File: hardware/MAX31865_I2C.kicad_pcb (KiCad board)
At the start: 2 copper layers, 25.4 x 27.9 mm, 3 parts

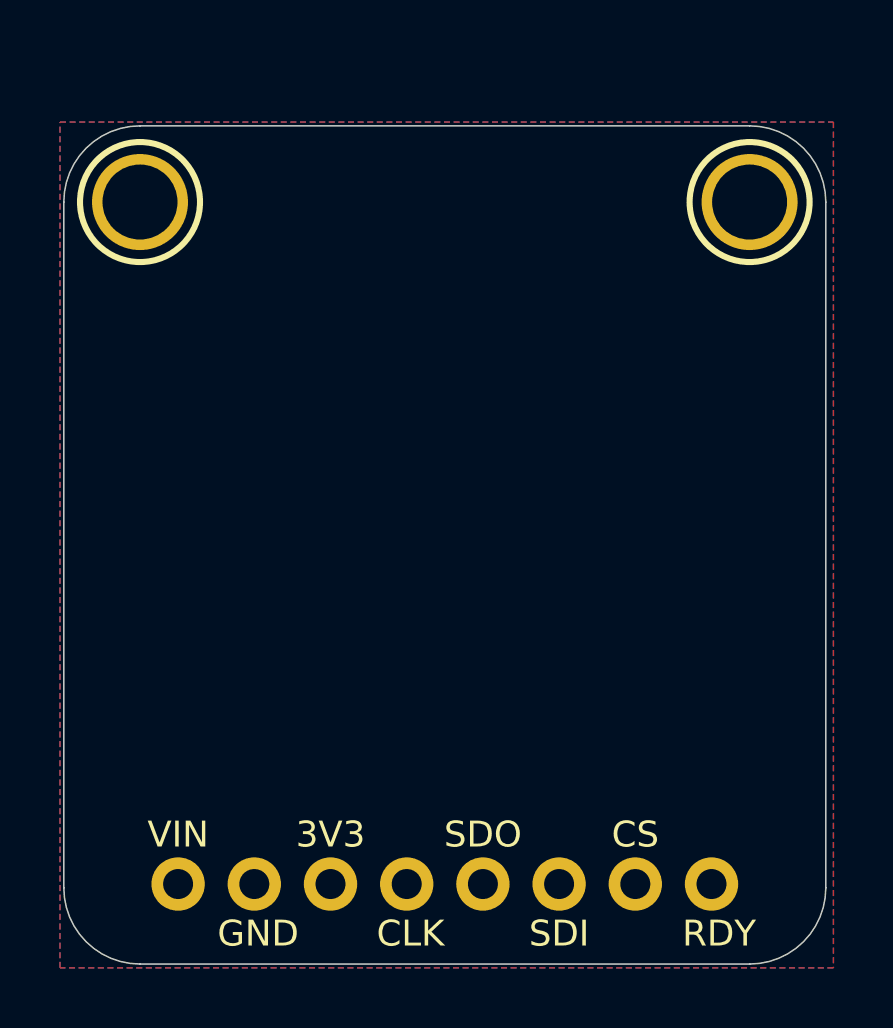
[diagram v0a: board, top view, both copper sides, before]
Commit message: added rough sketch of the adapter PCB
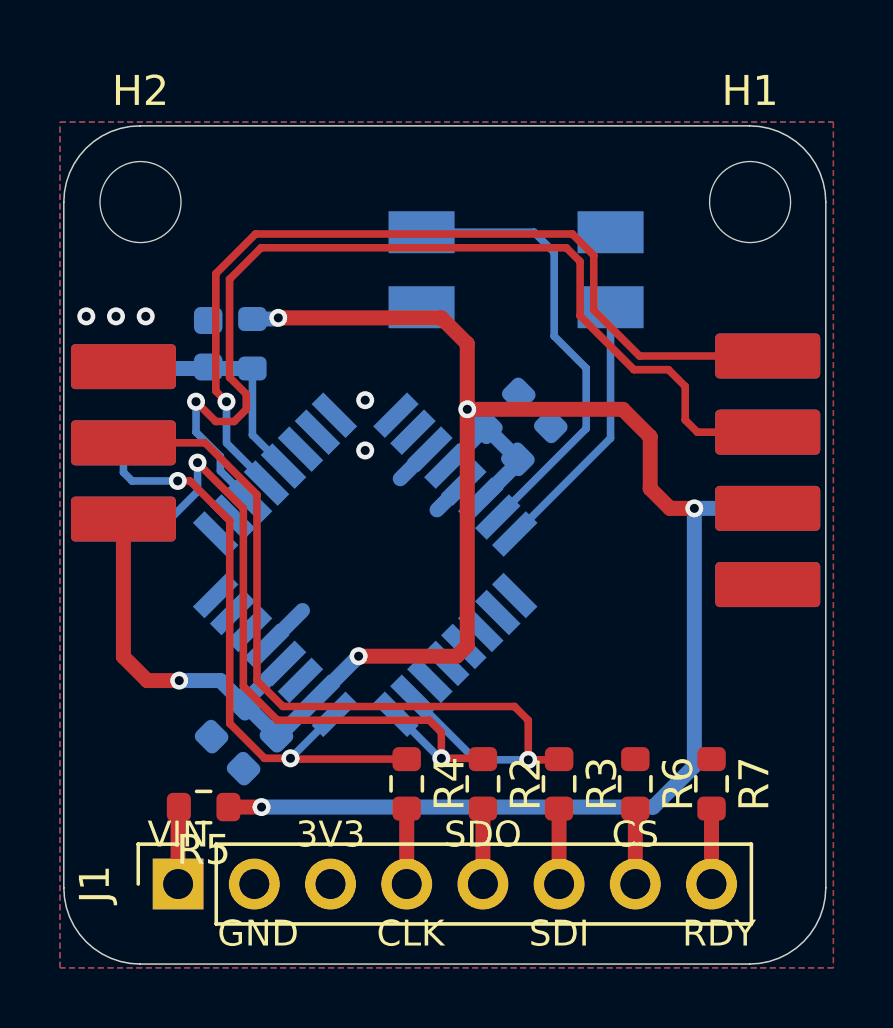
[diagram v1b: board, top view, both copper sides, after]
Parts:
- removed JP1: , 1X08_ROUND_70
- removed U$18, U$19: MOUNTINGHOLE2.5, MOUNTINGHOLE_2.5_PLATED
- added C1: 100n, Capacitor_SMD:C_0603_1608Metric, B.Cu at (140.6, 98.3)
- added C2: 100n, Capacitor_SMD:C_0603_1608Metric, B.Cu at (150.4, 100.5)
- added C3: 100n, Capacitor_SMD:C_0603_1608Metric, B.Cu at (142.3, 111.9)
- added C4: 100n, Capacitor_SMD:C_0603_1608Metric, B.Cu at (141.3, 110.8)
- added C5: 100n, Capacitor_SMD:C_0603_1608Metric, B.Cu at (151.5, 101.6)
- added H1: MountingHole, MountingHole:MountingHole_2.7mm, F.Cu at (158.7, 93.6)
- added H2: MountingHole, MountingHole:MountingHole_2.7mm, F.Cu at (138.4, 93.6)
- added J1: Conn_01x08, Connector_PinSocket_2.54mm:PinSocket_1x08_P2.54mm_Vertical, F.Cu at (139.6, 116.3)
- added J2: AVR-ISP-6, PinHeaderEdgeMount:PinHeader_2x03_P2.54mm_Edge, B.Cu at (135.8, 101.6)
- added J3: Conn_02x04_Odd_Even, PinHeaderEdgeMount:PinHeader_2x04_P2.54mm_Edge, B.Cu at (161.2, 102.5)
- added R1: 10k, Resistor_SMD:R_0603_1608Metric, B.Cu at (142.1, 98.3)
- added R2: 0, Resistor_SMD:R_0603_1608Metric, F.Cu at (149.8, 113.0)
- added R3: 0, Resistor_SMD:R_0603_1608Metric, F.Cu at (152.3, 113.0)
- added R4: 0, Resistor_SMD:R_0603_1608Metric, F.Cu at (147.2, 113.0)
- added R5: 0, Resistor_SMD:R_0603_1608Metric, F.Cu at (140.5, 113.7)
- added R6: 0, Resistor_SMD:R_0603_1608Metric, F.Cu at (154.9, 113.0)
- added R7: 0, Resistor_SMD:R_0603_1608Metric, F.Cu at (157.4, 113.0)
- added U1: ATmega48A-A, Package_QFP:TQFP-32_7x7mm_P0.8mm, B.Cu at (145.8, 105.7)
- added Y1: 16MHz, Crystal:Crystal_SMD_EuroQuartz_MQ-4Pin_7.0x5.0mm, B.Cu at (150.9, 95.8)
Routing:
- net +5V: track 0.00 -> 81.0 mm, vias 0 -> 6
- net /SDA: track 0.00 -> 33.3 mm, vias 0 -> 1
- net /SCL: track 0.00 -> 29.4 mm, vias 0 -> 1
- net /MOSI: track 0.00 -> 28.0 mm, vias 0 -> 1
- net /MISO: track 0.00 -> 23.5 mm, vias 0 -> 2
- net /SCK: track 0.00 -> 20.4 mm, vias 0 -> 2
- net Net-(U1-XTAL1/PB6): track 0.00 -> 15.2 mm
- net Net-(U1-XTAL2/PB7): track 0.00 -> 8.88 mm
- net /~{RESET}: track 0.00 -> 7.92 mm
- net GND: track 0.00 -> 4.36 mm, vias 0 -> 5
- net /VIN: track 0.00 -> 2.51 mm
- net /SDO: track 0.00 -> 2.51 mm
- net /SDI: track 0.00 -> 2.51 mm
- net /DRDY: track 0.00 -> 2.51 mm
- net /CS: track 0.00 -> 2.51 mm
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
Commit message: added caps for crystal
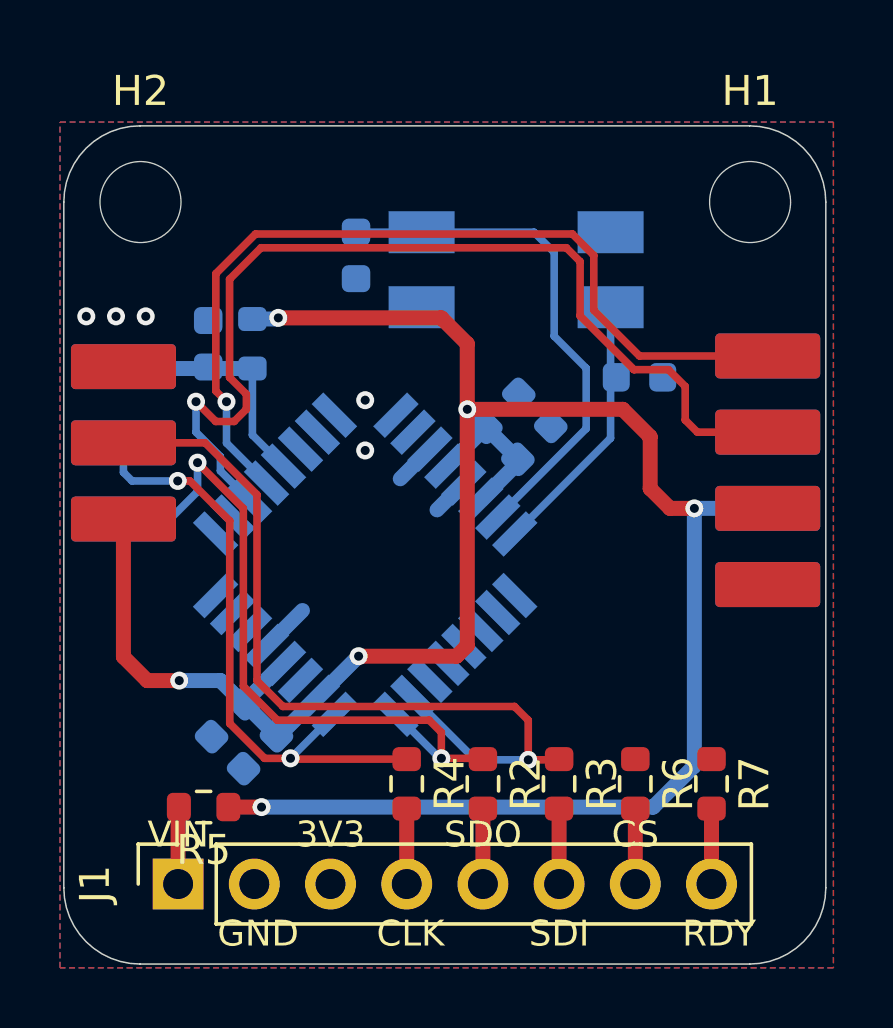
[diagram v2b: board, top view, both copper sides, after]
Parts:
- added C6: 22p, Capacitor_SMD:C_0603_1608Metric, B.Cu at (155.0, 99.4)
- added C7: 22p, Capacitor_SMD:C_0603_1608Metric, B.Cu at (145.5, 95.4)
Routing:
- net Net-(U1-XTAL1/PB6): track 15.2 -> 17.4 mm
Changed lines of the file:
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@@
+  )
+  (footprint "Capacitor_SMD:C_0603_1608Metric" (layer "B.Cu")
+    (at 154.9908 99.4156)
+    (descr "Capacitor SMD 0603 (1608 Metric), square (rectangular) end terminal, IPC_7351 nominal, (Body size source: IPC-SM-782 page 76, https://www.pcb-3d.com/wordpress/wp-content/uploads/ipc-sm-782a_amendment_1_and_2.pdf), generated with kicad-footprint-generator")
+    (tags "capacitor")
+    (property "Sheetfile" "MAX31865_I2C.kicad_sch")
+    (property "Sheetname" "")
+    (property "ki_description" "Unpolarized capacitor")
+    (property "ki_keywords" "cap capacitor")
+    (attr smd)
+    (fp_text reference "C6" (at 0 1.43) (layer "B.SilkS")
+        (effects (font (size 1 1) (thickness 0.15)) (justify mirror))
+    )
+    (fp_text value "22p" (at 0 -1.43) (layer "B.Fab")
+        (effects (font (size 1 1) (thickness 0.15)) (justify mirror))
+    )
+    (fp_text user "${REFERENCE}" (at 0 0) (layer "B.Fab")
+        (effects (font (size 0.4 0.4) (thickness 0.06)) (justify mirror))
+    )
+    (fp_line (start -0.14058 -0.51) (end 0.14058 -0.51)
+      (stroke (width 0.12) (type solid)) (layer "B.SilkS"))
+    (fp_line (start -0.14058 0.51) (end 0.14058 0.51)
+      (stroke (width 0.12) (type solid)) (layer "B.SilkS"))
+    (fp_line (start -1.48 -0.73) (end -1.48 0.73)
+      (stroke (width 0.05) (type solid)) (layer "B.CrtYd"))
+    (fp_line (start -1.48 0.73) (end 1.48 0.73)
+      (stroke (width 0.05) (type solid)) (layer "B.CrtYd"))
+    (fp_line (start 1.48 -0.73) (end -1.48 -0.73)
+      (stroke (width 0.05) (type solid)) (layer "B.CrtYd"))
+    (fp_line (start 1.48 0.73) (end 1.48 -0.73)
+      (stroke (width 0.05) (type solid)) (layer "B.CrtYd"))
+    (fp_line (start -0.8 -0.4) (end -0.8 0.4)
+      (stroke (width 0.1) (type solid)) (layer "B.Fab"))
+    (fp_line (start -0.8 0.4) (end 0.8 0.4)
+      (stroke (width 0.1) (type solid)) (layer "B.Fab"))
+    (fp_line (start 0.8 -0.4) (end -0.8 -0.4)
+      (stroke (width 0.1) (type solid)) (layer "B.Fab"))
+    (fp_line (start 0.8 0.4) (end 0.8 -0.4)
+      (stroke (width 0.1) (type solid)) (layer "B.Fab"))
+    (pad "1" smd roundrect (at -0.775 0) (size 0.9 0.95) (layers "B.Cu" "B.Paste" "B.Mask") (roundrect_rratio 0.25)
+      (net 34 "Net-(U1-XTAL2{slash}PB7)") (pintype "passive"))
+    (pad "2" smd roundrect (at 0.775 0) (size 0.9 0.95) (layers "B.Cu" "B.Paste" "B.Mask") (roundrect_rratio 0.25)
+      (net 1 "GND") (pintype "passive"))
+    (model "${KICAD6_3DMODEL_DIR}/Capacitor_SMD.3dshapes/C_0603_1608Metric.wrl"
+      (offset (xyz 0 0 0))
+      (scale (xyz 1 1 1))
+      (rotate (xyz 0 0 0))
+    )
   )
   (footprint "Capacitor_SMD:C_0603_1608Metric" (layer "B.Cu")
@@
       (net 27 "/~{RESET}") (pintype "passive"))
     (model "${KICAD6_3DMODEL_DIR}/Resistor_SMD.3dshapes/R_0603_1608Metric.wrl"
+      (offset (xyz 0 0 0))
+      (scale (xyz 1 1 1))
+      (rotate (xyz 0 0 0))
+    )
+  )
+  (footprint "Capacitor_SMD:C_0603_1608Metric" (layer "B.Cu")
+    (at 145.542 95.3516 -90)
+    (descr "Capacitor SMD 0603 (1608 Metric), square (rectangular) end terminal, IPC_7351 nominal, (Body size source: IPC-SM-782 page 76, https://www.pcb-3d.com/wordpress/wp-content/uploads/ipc-sm-782a_amendment_1_and_2.pdf), generated with kicad-footprint-generator")
+    (tags "capacitor")
+    (property "Sheetfile" "MAX31865_I2C.kicad_sch")
+    (property "Sheetname" "")
+    (property "ki_description" "Unpolarized capacitor")
+    (property "ki_keywords" "cap capacitor")
+    (attr smd)
+    (fp_text reference "C7" (at 0 1.43 90) (layer "B.SilkS")
+        (effects (font (size 1 1) (thickness 0.15)) (justify mirror))
+    )
+    (fp_text value "22p" (at 0 -1.43 90) (layer "B.Fab")
+        (effects (font (size 1 1) (thickness 0.15)) (justify mirror))
+    )
+    (fp_text user "${REFERENCE}" (at 0 0 90) (layer "B.Fab")
+        (effects (font (size 0.4 0.4) (thickness 0.06)) (justify mirror))
+    )
+    (fp_line (start -0.14058 -0.51) (end 0.14058 -0.51)
+      (stroke (width 0.12) (type solid)) (layer "B.SilkS"))
+    (fp_line (start -0.14058 0.51) (end 0.14058 0.51)
+      (stroke (width 0.12) (type solid)) (layer "B.SilkS"))
+    (fp_line (start -1.48 -0.73) (end -1.48 0.73)
+      (stroke (width 0.05) (type solid)) (layer "B.CrtYd"))
+    (fp_line (start -1.48 0.73) (end 1.48 0.73)
+      (stroke (width 0.05) (type solid)) (layer "B.CrtYd"))
+    (fp_line (start 1.48 -0.73) (end -1.48 -0.73)
+      (stroke (width 0.05) (type solid)) (layer "B.CrtYd"))
+    (fp_line (start 1.48 0.73) (end 1.48 -0.73)
+      (stroke (width 0.05) (type solid)) (layer "B.CrtYd"))
+    (fp_line (start -0.8 -0.4) (end -0.8 0.4)
+      (stroke (width 0.1) (type solid)) (layer "B.Fab"))
+    (fp_line (start -0.8 0.4) (end 0.8 0.4)
+      (stroke (width 0.1) (type solid)) (layer "B.Fab"))
+    (fp_line (start 0.8 -0.4) (end -0.8 -0.4)
+      (stroke (width 0.1) (type solid)) (layer "B.Fab"))
+    (fp_line (start 0.8 0.4) (end 0.8 -0.4)
+      (stroke (width 0.1) (type solid)) (layer "B.Fab"))
+    (pad "1" smd roundrect (at -0.775 0 270) (size 0.9 0.95) (layers "B.Cu" "B.Paste" "B.Mask") (roundrect_rratio 0.25)
+      (net 33 "Net-(U1-XTAL1{slash}PB6)") (pintype "passive"))
+    (pad "2" smd roundrect (at 0.775 0 270) (size 0.9 0.95) (layers "B.Cu" "B.Paste" "B.Mask") (roundrect_rratio 0.25)
+      (net 1 "GND") (pintype "passive"))
+    (model "${KICAD6_3DMODEL_DIR}/Capacitor_SMD.3dshapes/C_0603_1608Metric.wrl"
       (offset (xyz 0 0 0))
       (scale (xyz 1 1 1))
@@
   (segment (start 151.4748 94.5788) (end 152.146 95.25) (width 0.254) (layer "B.Cu") (net 33))
   (segment (start 153.2128 101.126427) (end 153.2128 99.1108) (width 0.254) (layer "B.Cu") (net 33))
+  (segment (start 147.7242 94.5766) (end 147.7264 94.5788) (width 0.254) (layer "B.Cu") (net 33))
   (segment (start 150.266217 104.07301) (end 153.2128 101.126427) (width 0.254) (layer "B.Cu") (net 33))
   (segment (start 147.7264 94.5788) (end 151.4748 94.5788) (width 0.254) (layer "B.Cu") (net 33))
   (segment (start 152.146 95.25) (end 152.146 98.044) (width 0.254) (layer "B.Cu") (net 33))
   (segment (start 152.146 98.044) (end 153.2128 99.1108) (width 0.254) (layer "B.Cu") (net 33))
+  (segment (start 145.542 94.5766) (end 147.7242 94.5766) (width 0.254) (layer "B.Cu") (net 33))
   (segment (start 150.831903 104.638695) (end 154.0264 101.444198) (width 0.254) (layer "B.Cu") (net 34))
   (segment (start 154.0264 101.444198) (end 154.0264 97.0788) (width 0.254) (layer "B.Cu") (net 34))

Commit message: connected CS and DRDY of MAX31865 module
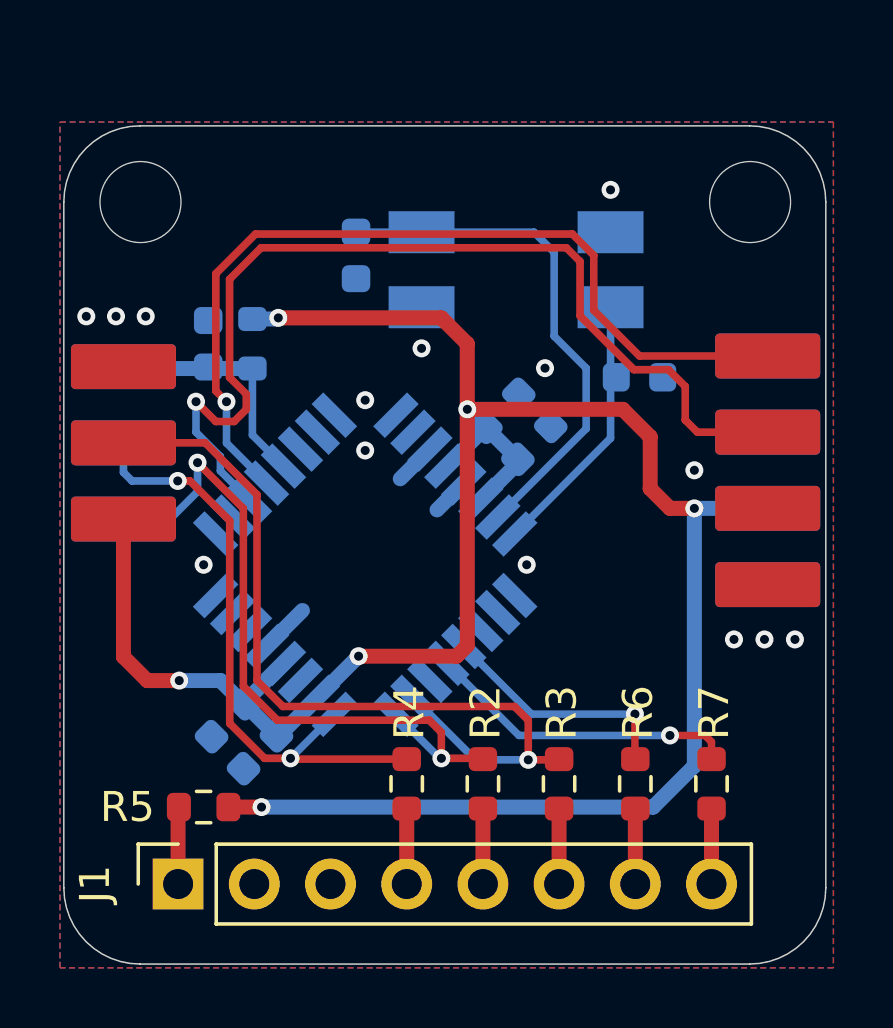
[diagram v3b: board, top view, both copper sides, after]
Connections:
- R6 pad 1: unconnected-(R6-Pad1) -> /M_CS
- R7 pad 1: unconnected-(R7-Pad1) -> /M_DRDY
- U1 pad 12: unconnected-(U1-PB0-Pad12) -> /M_CS
- U1 pad 13: unconnected-(U1-PB1-Pad13) -> /M_DRDY
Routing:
- net /M_DRDY: track 0.00 -> 10.5 mm, vias 0 -> 1
- net /M_CS: track 0.00 -> 8.14 mm, vias 0 -> 1
- net GND: vias 5 -> 14
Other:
- board text removed: "3V3"
- board text removed: "CLK"
- board text removed: "CS"
- board text removed: "GND"
- board text removed: "RDY"
- board text removed: "SDI"
- board text removed: "SDO"
- board text removed: "VIN"

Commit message: added template for schematic and cleaned PCB a tiny bit
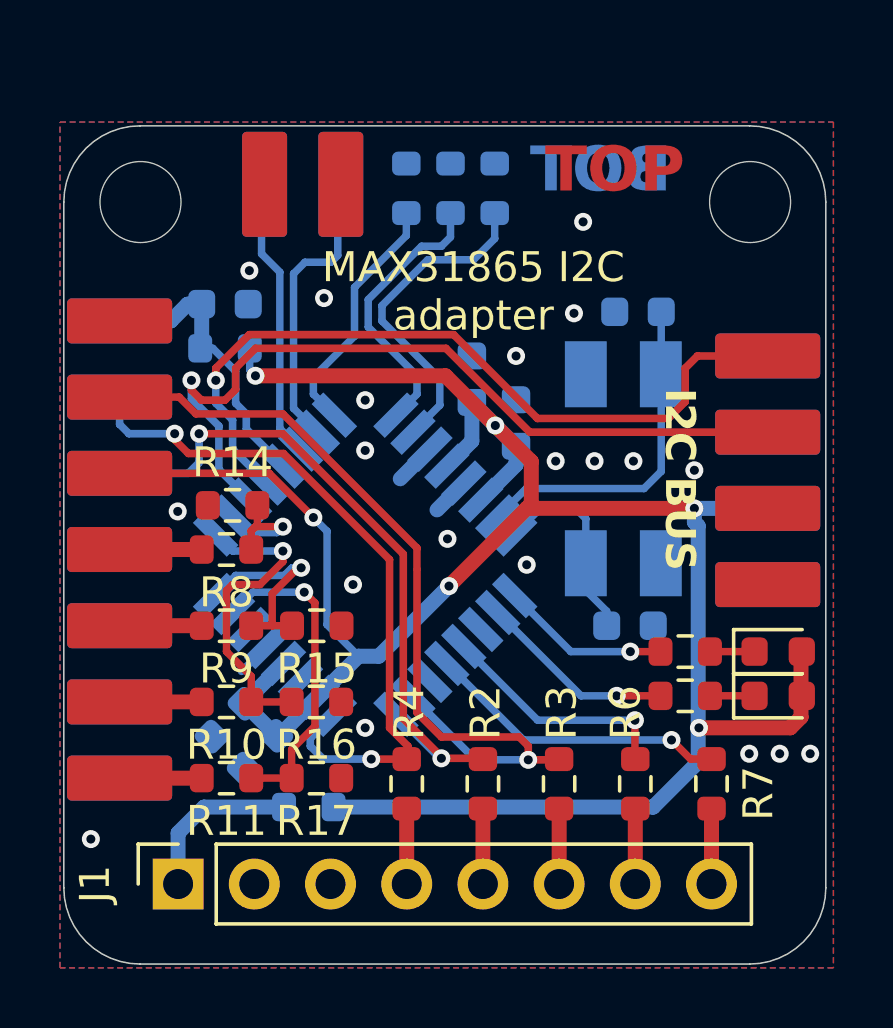
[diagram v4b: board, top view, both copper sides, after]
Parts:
- added D1: LED, LED_SMD:LED_0603_1608Metric, F.Cu at (159.6, 108.6)
- added D2: LED, LED_SMD:LED_0603_1608Metric, F.Cu at (159.6, 110.0)
- added J4: Conn_02x04_Odd_Even, PinHeaderEdgeMount:PinHeader_2x04_P2.54mm_Edge, F.Cu at (135.7, 109.0)
- added J5: Conn_02x02_Odd_Even, PinHeaderEdgeMount:PinHeader_2x02_P2.54mm_Edge, B.Cu at (143.8, 91.0)
- added R10: 0, Resistor_SMD:R_0603_1608Metric, F.Cu at (141.2, 110.2)
- added R11: 0, Resistor_SMD:R_0603_1608Metric, F.Cu at (141.2, 112.8)
- added R12: 2k2, Resistor_SMD:R_0603_1608Metric, F.Cu at (156.5, 110.0)
- added R13: 2k2, Resistor_SMD:R_0603_1608Metric, F.Cu at (156.5, 108.6)
- added R14: ~, Resistor_SMD:R_0603_1608Metric, F.Cu at (141.4, 103.7)
- added R15: ~, Resistor_SMD:R_0603_1608Metric, F.Cu at (144.2, 107.7)
- added R16: ~, Resistor_SMD:R_0603_1608Metric, F.Cu at (144.2, 110.2)
- added R17: ~, Resistor_SMD:R_0603_1608Metric, F.Cu at (144.2, 112.8)
- added R20: ~, Resistor_SMD:R_0603_1608Metric, B.Cu at (147.2, 93.1)
- added R21: ~, Resistor_SMD:R_0603_1608Metric, B.Cu at (148.7, 93.1)
- added R22: ~, Resistor_SMD:R_0603_1608Metric, B.Cu at (150.2, 93.1)
- added R8: 0, Resistor_SMD:R_0603_1608Metric, F.Cu at (141.2, 105.2)
- added R9: 0, Resistor_SMD:R_0603_1608Metric, F.Cu at (141.2, 107.7)
- R5: moved to B.Cu
- moved C7 9.58 mm to (154.9, 97.2), turned to 180 degrees
- moved C6 8.29 mm to (154.7, 107.7)
- moved Y1 7.54 mm to (154.5, 102.5), turned to 90 degrees
- moved R5 3.51 mm to (144.0, 113.7)
- moved C5 2.97 mm to (149.4, 99.5), turned to 90 degrees
- moved J2 1.53 mm to (135.7, 100.1)
- moved C1 1.43 mm to (141.2, 97.0), turned to 0 degrees
- moved R1 0.93 mm to (141.2, 98.5), turned to 180 degrees
- moved C2 0.61 mm to (150.9, 100.9), turned to 90 degrees
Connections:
- U1 pad 1: unconnected-(U1-PD3-Pad1) -> /ADDR1
- U1 pad 10: unconnected-(U1-PD6-Pad10) -> /LED1
- U1 pad 2: unconnected-(U1-PD4-Pad2) -> /ADDR2
- U1 pad 23: unconnected-(U1-PC0-Pad23) -> /GPIO3
- U1 pad 24: unconnected-(U1-PC1-Pad24) -> /GPIO1
- U1 pad 25: unconnected-(U1-PC2-Pad25) -> /GPIO2
- U1 pad 26: unconnected-(U1-PC3-Pad26) -> /GPIO0
- U1 pad 32: unconnected-(U1-PD2-Pad32) -> /ADDR0
- U1 pad 9: unconnected-(U1-PD5-Pad9) -> /LED0
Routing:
- net /ADDR2: track 0.00 -> 10.9 mm
- net /GPIO3: track 0.00 -> 10.7 mm, vias 0 -> 1
- net /GPIO2: track 0.00 -> 10.6 mm, vias 0 -> 1
- net /TXD: track 0.00 -> 9.73 mm
- net /RXD: track 0.00 -> 9.38 mm
- net /ADDR1: track 0.00 -> 9.22 mm
- net /ADDR0: track 0.00 -> 8.31 mm
- net /GPIO1: track 0.00 -> 6.98 mm, vias 0 -> 1
- net /SDA: track 33.3 -> 26.8 mm
- net /LED1: track 0.00 -> 6.57 mm, vias 0 -> 1
- net Net-(U1-XTAL1/PB6): track 17.4 -> 11.4 mm
- net /LED0: track 0.00 -> 5.63 mm, vias 0 -> 1
- net /GPIO0: track 0.00 -> 4.64 mm, vias 0 -> 1
- net /SCL: track 29.4 -> 26.1 mm
- net /SCK: track 20.4 -> 23.5 mm
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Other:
- board text added: "BOT"
- board text added: "I2C BUS"
- board text added: "JS2023"
- board text added: "MAX31865 I2C adapter"
- board text added: "TOP"
